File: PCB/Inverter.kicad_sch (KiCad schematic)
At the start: 79 parts, among them J1 Conn_01x02, J2 Conn_01x05_Pin, J3 Conn_01x05_Pin, Q1 STP110N8F6, Q2 STP110N8F6, Q3 STP110N8F6, Q4 STP110N8F6, Q5 STP110N8F6, Q6 STP110N8F6, U1 XL7015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

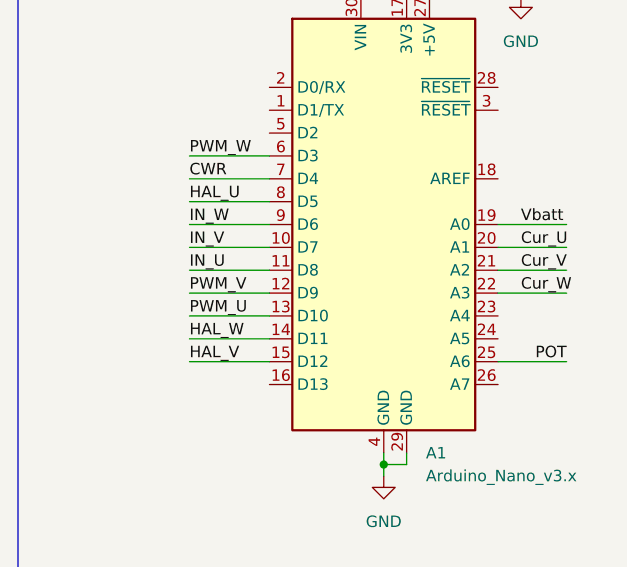
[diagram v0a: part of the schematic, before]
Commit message: Change#012
The outputs on the board for setting the operation of half-bridges have been changed, as well as the inputs for Hall sensors, so that they are in the space of one port and read by one line of code, and the interrupts for level changes in the code have been changed to accommodate this feature.
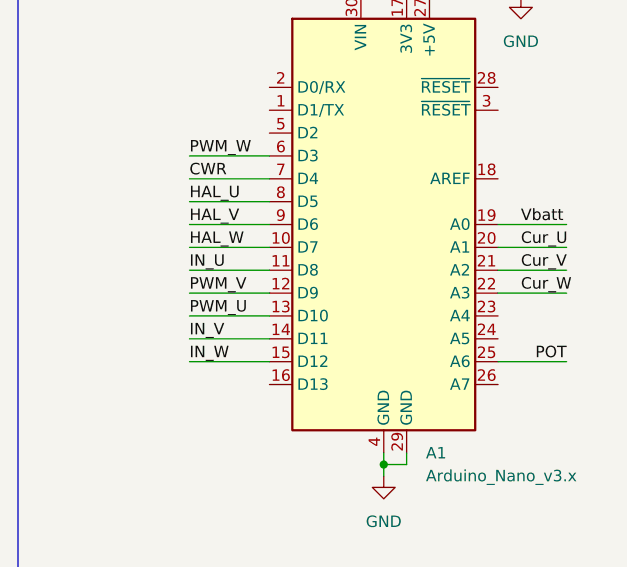
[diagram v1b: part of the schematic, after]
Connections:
- net HAL_V: now also A1.9 (D6); no longer A1.15 (D12)
- net HAL_W: now also A1.10 (D7); no longer A1.14 (D11)
- net IN_V: now also A1.14 (D11); no longer A1.10 (D7)
- net IN_W: now also A1.15 (D12); no longer A1.9 (D6)
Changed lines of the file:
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@@
+	(wire
+		(pts
+			(xy 31.75 114.3) (xy 40.64 114.3)
+		)
+		(stroke
+			(width 0)
+			(type default)
+		)
+	)
 	(wire
 		(pts
@@
 	(wire
 		(pts
+			(xy 31.75 127) (xy 40.64 127)
+		)
+		(stroke
+			(width 0)
+			(type default)
+		)
+	)
+	(wire
+		(pts
 			(xy 127 115.57) (xy 127 114.3)
 		)
@@
 	(wire
 		(pts
-			(xy 31.75 127) (xy 40.64 127)
-		)
-		(stroke
-			(width 0)
-			(type default)
-		)
-	)
-	(wire
-		(pts
 			(xy 39.37 40.64) (xy 49.53 40.64)
 		)
@@
 	(wire
 		(pts
+			(xy 31.75 116.84) (xy 40.64 116.84)
+		)
+		(stroke
+			(width 0)
+			(type default)
+		)
+	)
+	(wire
+		(pts
 			(xy 170.18 151.13) (xy 189.23 151.13)
 		)
@@
 	(wire
 		(pts
+			(xy 31.75 129.54) (xy 40.64 129.54)
+		)
+		(stroke
+			(width 0)
+			(type default)
+		)
+	)
+	(wire
+		(pts
 			(xy 269.24 154.94) (xy 264.16 154.94)
 		)
@@
 	(wire
 		(pts
-			(xy 31.75 116.84) (xy 40.64 116.84)
-		)
-		(stroke
-			(width 0)
-			(type default)
-		)
-	)
-	(wire
-		(pts
 			(xy 241.3 43.18) (xy 246.38 43.18)
 		)
@@
 	(wire
 		(pts
-			(xy 31.75 114.3) (xy 40.64 114.3)
-		)
-		(stroke
-			(width 0)
-			(type default)
-		)
-	)
-	(wire
-		(pts
 			(xy 53.34 38.1) (xy 53.34 40.64)
 		)
@@
 		(pts
 			(xy 245.11 127) (xy 245.11 130.81)
-		)
-		(stroke
-			(width 0)
-			(type default)
-		)
-	)
-	(wire
-		(pts
-			(xy 31.75 129.54) (xy 40.64 129.54)
 		)
 		(stroke
@@
 		)
 	)
-	(label "HAL_W"
-		(at 31.75 127 0)
-		(effects
-			(font
-				(size 1.27 1.27)
-			)
-			(justify left bottom)
-		)
-	)
 	(label "W_OUT"
 		(at 123.19 82.55 270)
@@
 		)
 	)
-	(label "IN_W"
-		(at 31.75 114.3 0)
-		(effects
-			(font
-				(size 1.27 1.27)
-			)
-			(justify left bottom)
-		)
-	)
-	(label "IN_V"
-		(at 31.75 116.84 0)
-		(effects
-			(font
-				(size 1.27 1.27)
-			)
-			(justify left bottom)
-		)
-	)
 	(label "PWM_W"
 		(at 209.55 139.7 0)
@@
 		)
 	)
+	(label "IN_V"
+		(at 31.75 127 0)
+		(effects
+			(font
+				(size 1.27 1.27)
+			)
+			(justify left bottom)
+		)
+	)
 	(label "U_IN"
 		(at 165.1 24.13 180)
@@
 		)
 	)
+	(label "HAL_V"
+		(at 31.75 114.3 0)
+		(effects
+			(font
+				(size 1.27 1.27)
+			)
+			(justify left bottom)
+		)
+	)
 	(label "Vin"
 		(at 115.57 26.67 0)
@@
 		)
 	)
+	(label "HAL_W"
+		(at 31.75 116.84 0)
+		(effects
+			(font
+				(size 1.27 1.27)
+			)
+			(justify left bottom)
+		)
+	)
 	(label "Cur_W"
 		(at 68.58 121.92 0)
@@
 		)
 	)
+	(label "IN_W"
+		(at 31.75 129.54 0)
+		(effects
+			(font
+				(size 1.27 1.27)
+			)
+			(justify left bottom)
+		)
+	)
 	(label "W_IN"
 		(at 165.1 116.84 180)
@@
 		(effects
 			(font
-				(size 1.27 1.27)
-			)
-			(justify left bottom)
-		)
-	)
-	(label "HAL_V"
-		(at 31.75 129.54 0)
-		(effects
-			(font

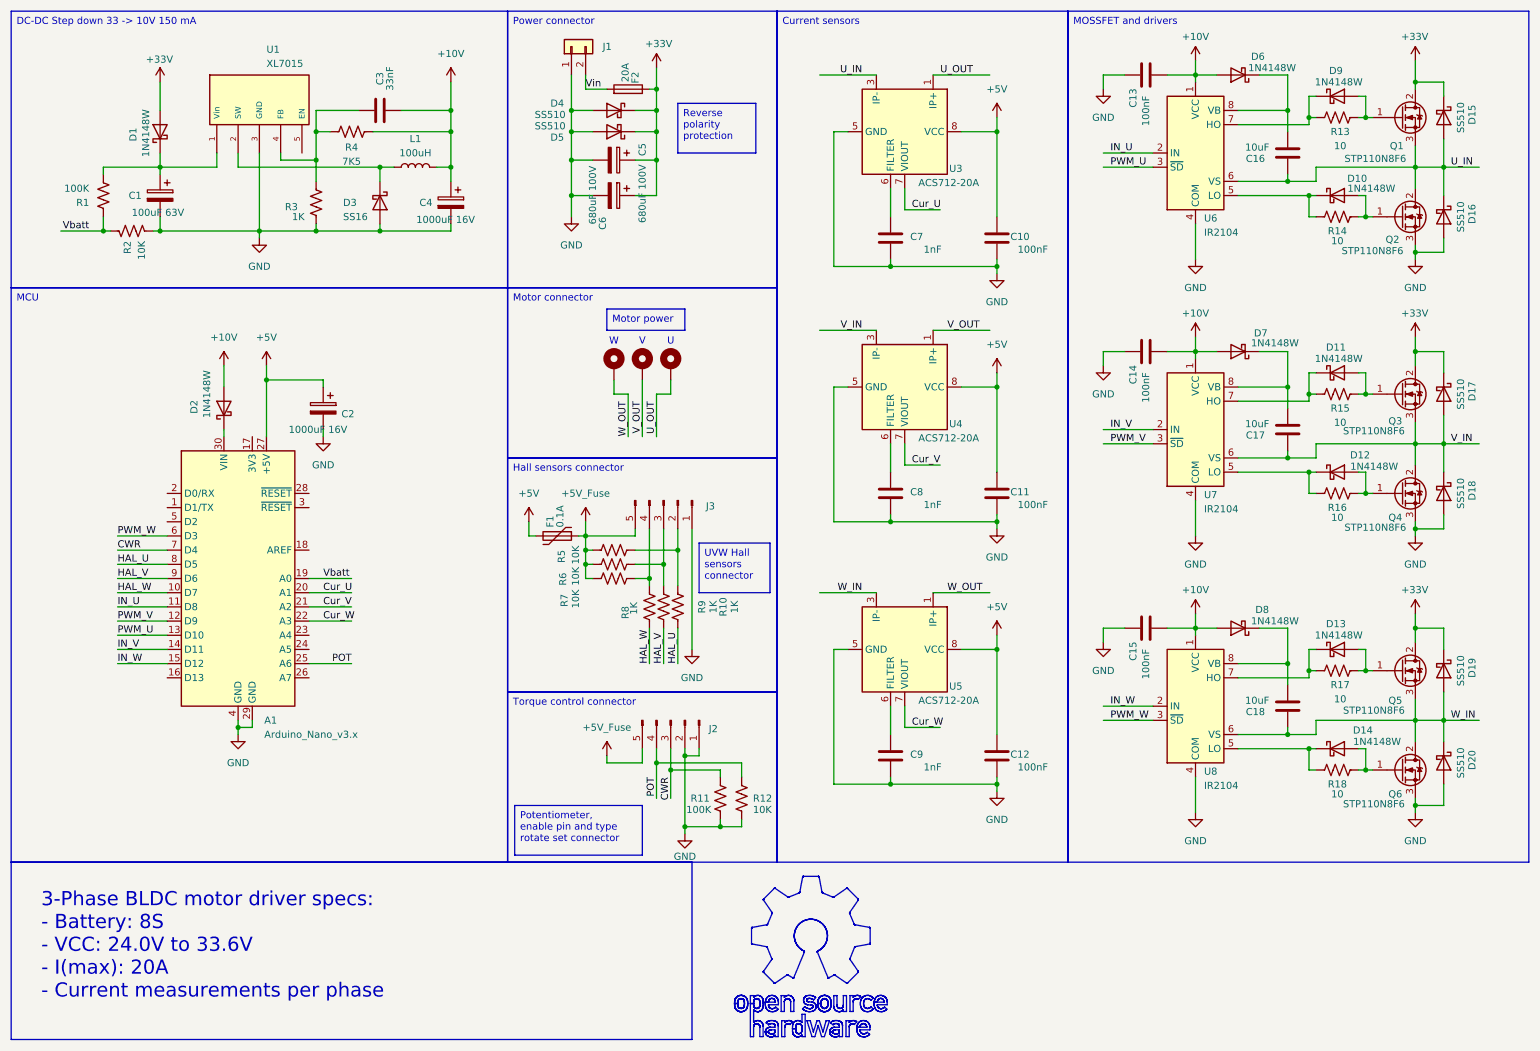
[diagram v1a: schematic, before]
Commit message: Change#014
Added capacitors for the outputs from the Hall sensors.
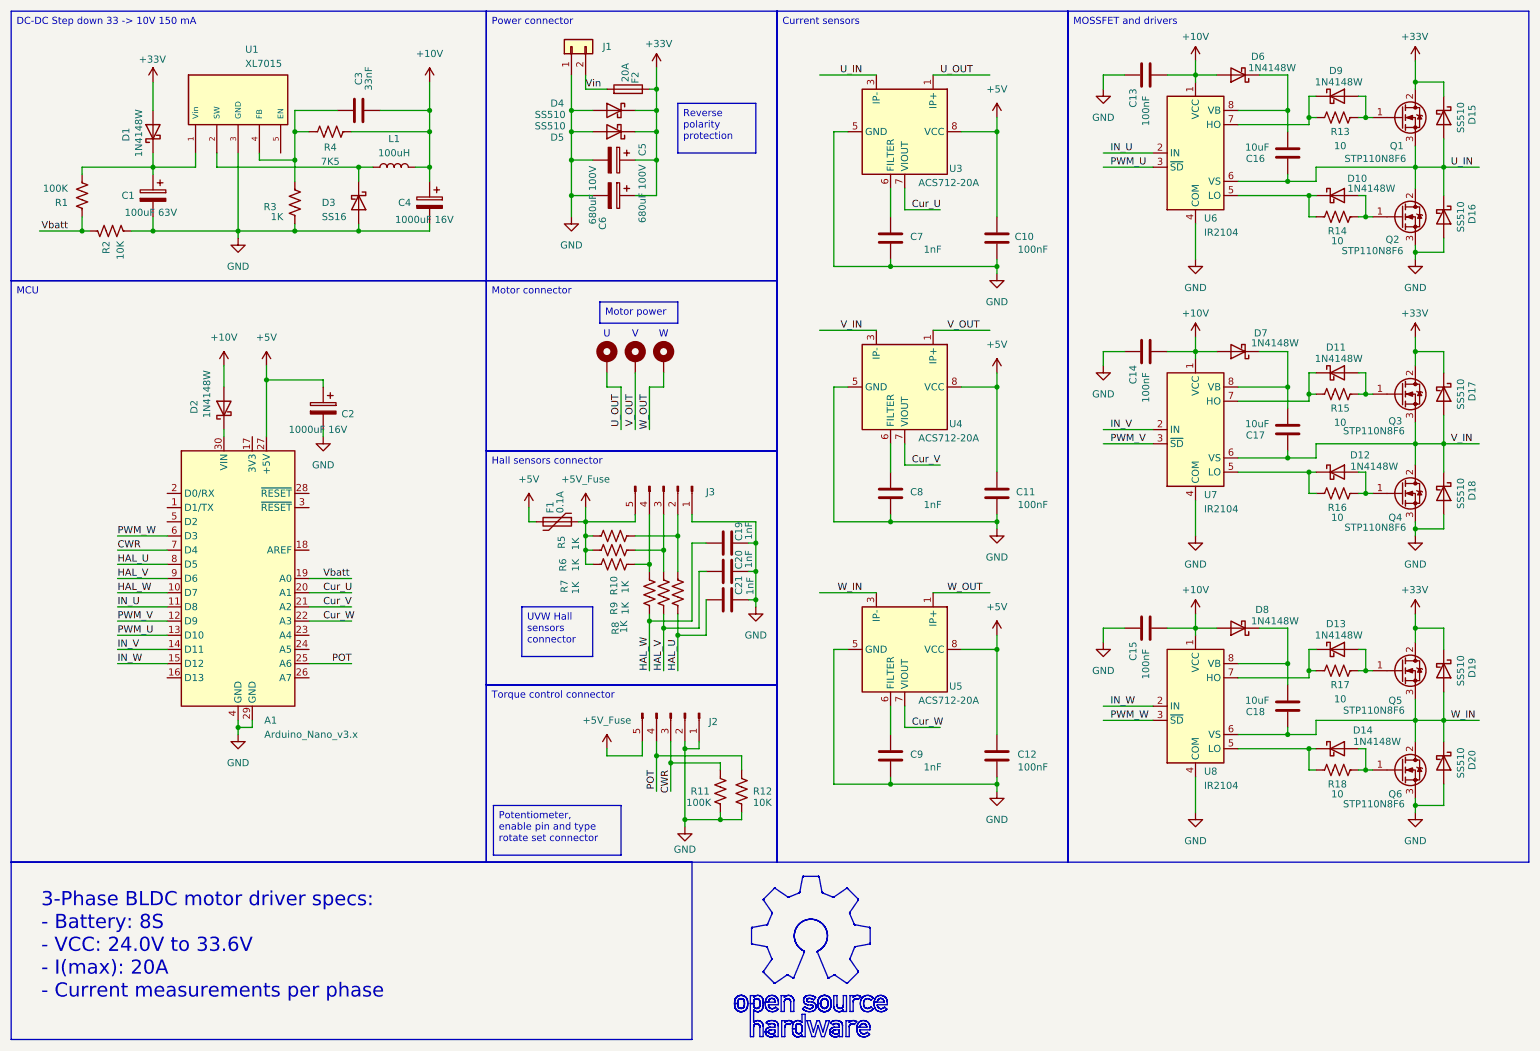
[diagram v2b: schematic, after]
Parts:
- added C19, C20, C21: 1nF, Capacitor_SMD:C_0805_2012Metric_Pad1.18x1.45mm_HandSolder, symbol Device:C
- R5, R6, R7: value 10K -> 1K
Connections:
- net GND: now also C19.2, C20.2, C21.2
- net HAL_U: now also C21.1
- net HAL_V: now also C20.1
- net HAL_W: now also C19.1
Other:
- moved on the sheet: C1, C3, C4, D1, D3, F1, J2, J3, L1, R1, R10, R11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
